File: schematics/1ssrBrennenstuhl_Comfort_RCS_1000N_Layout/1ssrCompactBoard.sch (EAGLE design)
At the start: 20 parts, among them K1 AQG12105

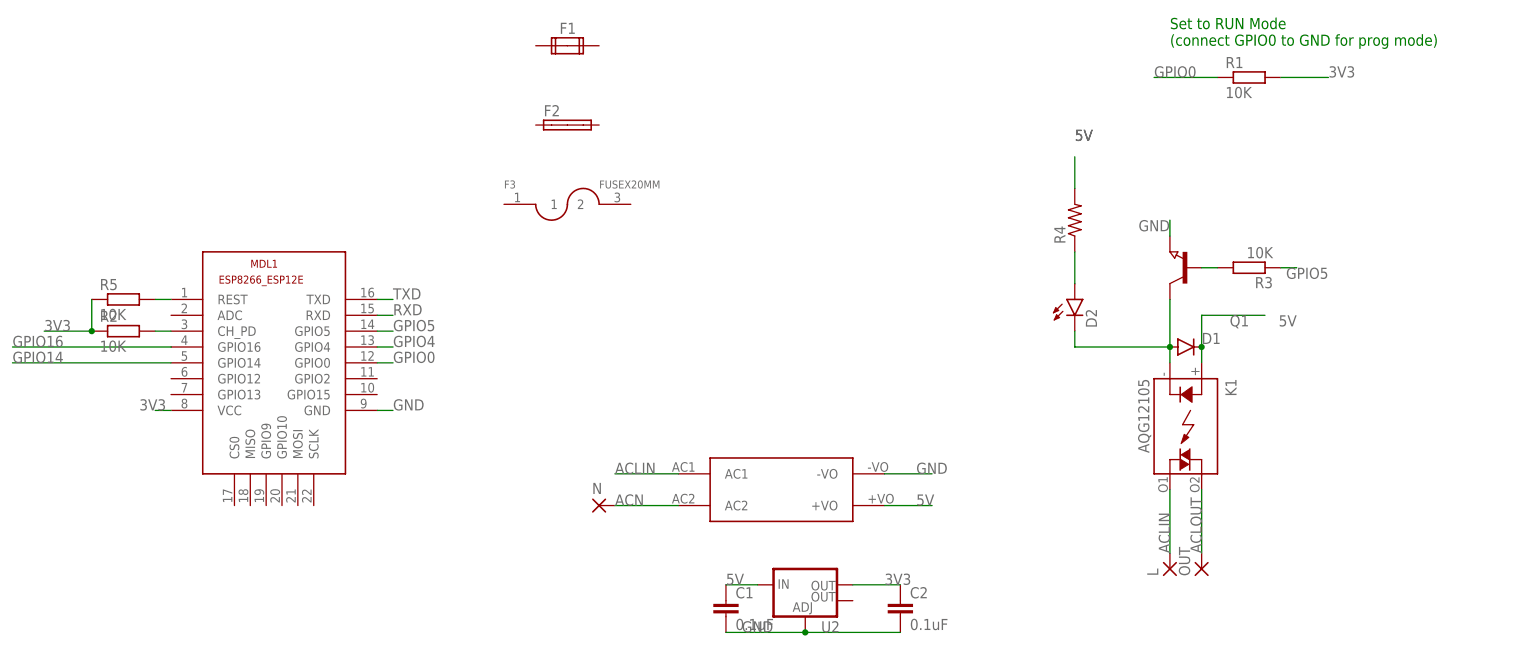
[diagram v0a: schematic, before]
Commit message: placed fuse on pcb
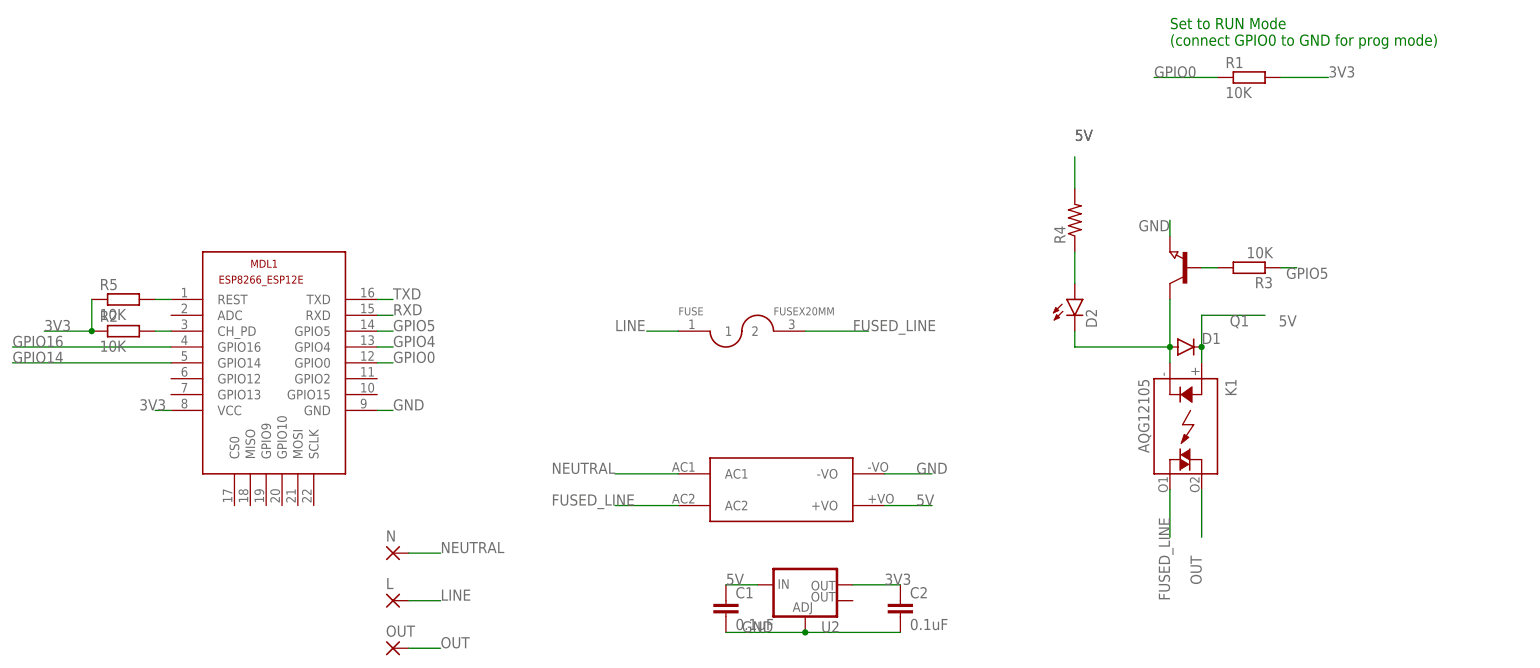
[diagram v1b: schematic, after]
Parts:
- removed F1: (no value), special:FUSE2P
- removed F2: (no value), fuse:SHK20L
- removed F3: FUSEX20MM, SparkFun-Passives:FUSEX20MM
- added FUSE: FUSEX20MM, SparkFun-Passives:FUSEX20MM
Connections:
- net ACLOUT renamed OUT
- removed net ACLIN: K1.DS2, L.P, U$4.AC1
- removed net ACN: N.P, U$4.AC2
- new net FUSED_LINE: FUSE.2, K1.DS2, U$4.AC2
- new net LINE: FUSE.1, L.P
- new net NEUTRAL: N.P, U$4.AC1
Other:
- moved on the sheet: L, N, OUT
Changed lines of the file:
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@@
 <part name="D2" library="SparkFun-LED" deviceset="LED" device="0603"/>
 <part name="R4" library="SparkFun-Resistors" deviceset="RESISTOR" device="0603"/>
-<part name="F1" library="special" deviceset="FUSE2P" device=""/>
-<part name="F2" library="fuse" deviceset="SHK20L" device=""/>
-<part name="F3" library="SparkFun-Passives" deviceset="FUSE" device="X20MM"/>
+<part name="FUSE" library="SparkFun-Passives" deviceset="FUSE" device="X20MM"/>
 </parts>
 <sheets>
@@
 <instance part="MDL1" gate="G$1" x="12.7" y="35.56"/>
 <instance part="R1" gate="G$1" x="162.56" y="78.74"/>
-<instance part="N" gate="P" x="58.42" y="10.16"/>
-<instance part="L" gate="P" x="149.86" y="0" rot="R90"/>
-<instance part="OUT" gate="P" x="154.94" y="0" rot="R90"/>
+<instance part="N" gate="P" x="25.4" y="2.54"/>
+<instance part="L" gate="P" x="25.4" y="-5.08"/>
+<instance part="OUT" gate="P" x="25.4" y="-12.7"/>
 <instance part="D2" gate="G$1" x="134.62" y="43.18"/>
 <instance part="R4" gate="G$1" x="134.62" y="55.88" rot="R90"/>
-<instance part="F1" gate="G$1" x="53.34" y="83.82"/>
-<instance part="F2" gate="G$1" x="53.34" y="71.12"/>
-<instance part="F3" gate="G$1" x="53.34" y="58.42"/>
+<instance part="FUSE" gate="G$1" x="81.28" y="38.1"/>
 </instances>
 <busses>
@@
 </segment>
 </net>
-<net name="ACN" class="1">
-<segment>
-<pinref part="U$4" gate="G$1" pin="AC2"/>
-<wire x1="60.96" y1="10.16" x2="71.12" y2="10.16" width="0.1524" layer="91"/>
-<label x="60.96" y="10.16" size="1.778" layer="95"/>
-<pinref part="N" gate="P" pin="P"/>
-</segment>
-</net>
 <net name="N$6" class="0">
 <segment>
@@
 </segment>
 </net>
-<net name="ACLIN" class="1">
-<segment>
-<pinref part="K1" gate="A" pin="DS2"/>
-<wire x1="149.86" y1="12.7" x2="149.86" y2="2.54" width="0.1524" layer="91"/>
-<label x="149.86" y="2.54" size="1.778" layer="95" rot="R90"/>
-<pinref part="L" gate="P" pin="P"/>
-</segment>
-<segment>
-<pinref part="U$4" gate="G$1" pin="AC1"/>
-<wire x1="60.96" y1="15.24" x2="71.12" y2="15.24" width="0.1524" layer="91"/>
-<label x="60.96" y="15.24" size="1.778" layer="95"/>
-</segment>
-</net>
-<net name="ACLOUT" class="1">
-<segment>
-<pinref part="K1" gate="A" pin="DS1"/>
-<wire x1="154.94" y1="12.7" x2="154.94" y2="2.54" width="0.1524" layer="91"/>
-<label x="154.94" y="2.54" size="1.778" layer="95" rot="R90"/>
-<pinref part="OUT" gate="P" pin="P"/>
-</segment>
-</net>
 <net name="N$1" class="0">
 <segment>
@@
 </segment>
 </net>
+<net name="NEUTRAL" class="1">
+<segment>
+<pinref part="N" gate="P" pin="P"/>
+<wire x1="27.94" y1="2.54" x2="33.02" y2="2.54" width="0.1524" layer="91"/>
+<label x="33.02" y="2.54" size="1.778" layer="95"/>
+</segment>
+<segment>
+<pinref part="U$4" gate="G$1" pin="AC1"/>
+<wire x1="71.12" y1="15.24" x2="60.96" y2="15.24" width="0.1524" layer="91"/>
+<label x="50.8" y="15.24" size="1.778" layer="95"/>
+</segment>
+</net>
+<net name="LINE" class="1">
+<segment>
+<pinref part="L" gate="P" pin="P"/>
+<wire x1="27.94" y1="-5.08" x2="33.02" y2="-5.08" width="0.1524" layer="91"/>
+<label x="33.02" y="-5.08" size="1.778" layer="95"/>
+</segment>
+<segment>
+<pinref part="FUSE" gate="G$1" pin="1"/>
+<wire x1="71.12" y1="38.1" x2="66.04" y2="38.1" width="0.1524" layer="91"/>
+<label x="60.96" y="38.1" size="1.778" layer="95"/>
+</segment>
+</net>
+<net name="OUT" class="1">
+<segment>
+<pinref part="OUT" gate="P" pin="P"/>
+<wire x1="27.94" y1="-12.7" x2="33.02" y2="-12.7" width="0.1524" layer="91"/>
+<label x="33.02" y="-12.7" size="1.778" layer="95"/>
+</segment>
+<segment>
+<pinref part="K1" gate="A" pin="DS1"/>
+<wire x1="154.94" y1="12.7" x2="154.94" y2="5.08" width="0.1524" layer="91"/>
+<label x="154.94" y="-2.54" size="1.778" layer="95" rot="R90"/>
+</segment>
+</net>
+<net name="FUSED_LINE" class="1">
+<segment>
+<pinref part="U$4" gate="G$1" pin="AC2"/>
+<wire x1="71.12" y1="10.16" x2="60.96" y2="10.16" width="0.1524" layer="91"/>
+<label x="50.8" y="10.16" size="1.778" layer="95"/>
+</segment>
+<segment>
+<pinref part="K1" gate="A" pin="DS2"/>
+<wire x1="149.86" y1="12.7" x2="149.86" y2="5.08" width="0.1524" layer="91"/>
+<label x="149.86" y="-5.08" size="1.778" layer="95" rot="R90"/>
+</segment>
+<segment>
+<pinref part="FUSE" gate="G$1" pin="2"/>
+<wire x1="91.44" y1="38.1" x2="101.6" y2="38.1" width="0.1524" layer="91"/>
+<label x="99.06" y="38.1" size="1.778" layer="95"/>
+</segment>
+</net>

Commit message: board routing work in progress
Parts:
- added J1: (no value), SparkFun-Connectors:M02PTH3
- added R6: 10K, resistor:R-EU_R0805
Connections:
- net 3V3: now also R6.2
- net GND: now also J1.1
- net GPIO4: now also J1.2, R6.1
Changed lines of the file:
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@@
 <layer number="112" name="tSilk" color="7" fill="1" visible="yes" active="yes"/>
 <layer number="113" name="IDFDebug" color="4" fill="1" visible="yes" active="yes"/>
+<layer number="114" name="Badge_Outline" color="7" fill="1" visible="yes" active="yes"/>
+<layer number="115" name="ReferenceISLANDS" color="7" fill="1" visible="yes" active="yes"/>
 <layer number="116" name="Patch_BOT" color="9" fill="4" visible="yes" active="yes"/>
 <layer number="118" name="Rect_Pads" color="7" fill="1" visible="yes" active="yes"/>
@@
 <part name="R4" library="SparkFun-Resistors" deviceset="RESISTOR" device="0603"/>
 <part name="FUSE" library="SparkFun-Passives" deviceset="FUSE" device="X20MM"/>
+<part name="R6" library="resistor" deviceset="R-EU_" device="R0805" value="10K"/>
+<part name="J1" library="SparkFun-Connectors" deviceset="M02" device="PTH3"/>
 </parts>
 <sheets>
@@
 <instance part="R4" gate="G$1" x="134.62" y="55.88" rot="R90"/>
 <instance part="FUSE" gate="G$1" x="81.28" y="38.1"/>
+<instance part="R6" gate="G$1" x="25.4" y="73.66"/>
+<instance part="J1" gate="G$1" x="2.54" y="71.12"/>
 </instances>
 <busses>
@@
 <wire x1="167.64" y1="78.74" x2="175.26" y2="78.74" width="0.1524" layer="91"/>
 <label x="175.26" y="78.74" size="1.778" layer="95"/>
+</segment>
+<segment>
+<pinref part="R6" gate="G$1" pin="2"/>
+<wire x1="30.48" y1="73.66" x2="38.1" y2="73.66" width="0.1524" layer="91"/>
+<label x="33.02" y="73.66" size="1.778" layer="95"/>
 </segment>
 </net>
@@
 <label x="25.4" y="25.4" size="1.778" layer="95"/>
 </segment>
+<segment>
+<pinref part="J1" gate="G$1" pin="1"/>
+<wire x1="10.16" y1="71.12" x2="20.32" y2="71.12" width="0.1524" layer="91"/>
+<label x="15.24" y="71.12" size="1.778" layer="95"/>
+</segment>
 </net>
 <net name="5V" class="0">
@@
 <wire x1="157.48" y1="78.74" x2="147.32" y2="78.74" width="0.1524" layer="91"/>
 <label x="147.32" y="78.74" size="1.778" layer="95"/>
-</segment>
-</net>
-<net name="GPIO4" class="0">
-<segment>
-<pinref part="MDL1" gate="G$1" pin="GPIO4"/>
-<wire x1="22.86" y1="35.56" x2="25.4" y2="35.56" width="0.1524" layer="91"/>
-<label x="25.4" y="35.56" size="1.778" layer="95"/>
 </segment>
 </net>
@@
 </segment>
 </net>
+<net name="GPIO4" class="0">
+<segment>
+<pinref part="MDL1" gate="G$1" pin="GPIO4"/>
+<wire x1="22.86" y1="35.56" x2="25.4" y2="35.56" width="0.1524" layer="91"/>
+<label x="25.4" y="35.56" size="1.778" layer="95"/>
+</segment>
+<segment>
+<pinref part="J1" gate="G$1" pin="2"/>
+<wire x1="10.16" y1="73.66" x2="15.24" y2="73.66" width="0.1524" layer="91"/>
+<label x="15.24" y="78.74" size="1.778" layer="95"/>
+<pinref part="R6" gate="G$1" pin="1"/>
+<wire x1="15.24" y1="73.66" x2="20.32" y2="73.66" width="0.1524" layer="91"/>
+<wire x1="15.24" y1="73.66" x2="15.24" y2="78.74" width="0.1524" layer="91"/>
+<junction x="15.24" y="73.66"/>
+</segment>
+</net>

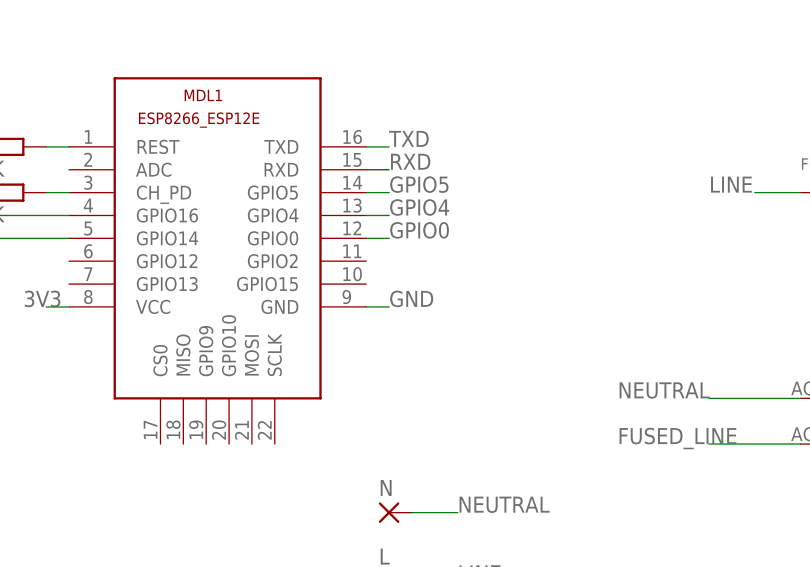
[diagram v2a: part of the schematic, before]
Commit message: added missing connection on pin gpio15
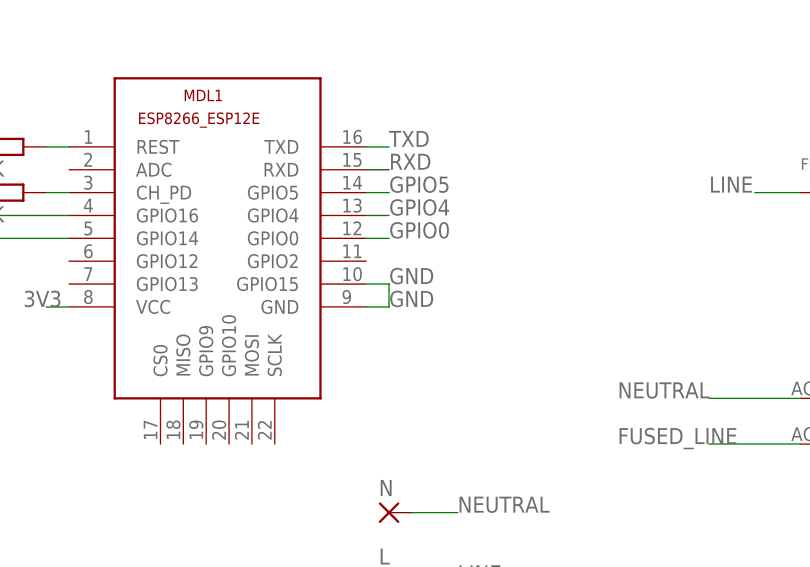
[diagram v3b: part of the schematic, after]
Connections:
- net GND: now also MDL1.GPIO15
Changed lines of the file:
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@@
 <?xml version="1.0" encoding="utf-8"?>
 <!DOCTYPE eagle SYSTEM "eagle.dtd">
-<eagle version="7.5.0">
+<eagle version="7.6.0">
 <drawing>
 <settings>
@@
 </segment>
 <segment>
+<pinref part="J1" gate="G$1" pin="1"/>
+<wire x1="10.16" y1="71.12" x2="20.32" y2="71.12" width="0.1524" layer="91"/>
+<label x="15.24" y="71.12" size="1.778" layer="95"/>
+</segment>
+<segment>
+<pinref part="MDL1" gate="G$1" pin="GPIO15"/>
+<wire x1="22.86" y1="27.94" x2="25.4" y2="27.94" width="0.1524" layer="91"/>
+<label x="25.4" y="27.94" size="1.778" layer="95"/>
 <pinref part="MDL1" gate="G$1" pin="GND"/>
 <wire x1="22.86" y1="25.4" x2="25.4" y2="25.4" width="0.1524" layer="91"/>
 <label x="25.4" y="25.4" size="1.778" layer="95"/>
-</segment>
-<segment>
-<pinref part="J1" gate="G$1" pin="1"/>
-<wire x1="10.16" y1="71.12" x2="20.32" y2="71.12" width="0.1524" layer="91"/>
-<label x="15.24" y="71.12" size="1.778" layer="95"/>
+<wire x1="25.4" y1="27.94" x2="25.4" y2="25.4" width="0.1524" layer="91"/>
 </segment>
 </net>
